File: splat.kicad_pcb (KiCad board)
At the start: 2 copper layers, 40 x 70 mm, 47 parts, among them J1 BATT, J2 EXT_SW, J3 Micro_SD_Card, J4 PYRO1, J5 PYRO3, J6 PYRO2, J7 PYRO3, J8 Conn_01x04, Q1 NTR4501NT1G, Q2 NTR4501NT1G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

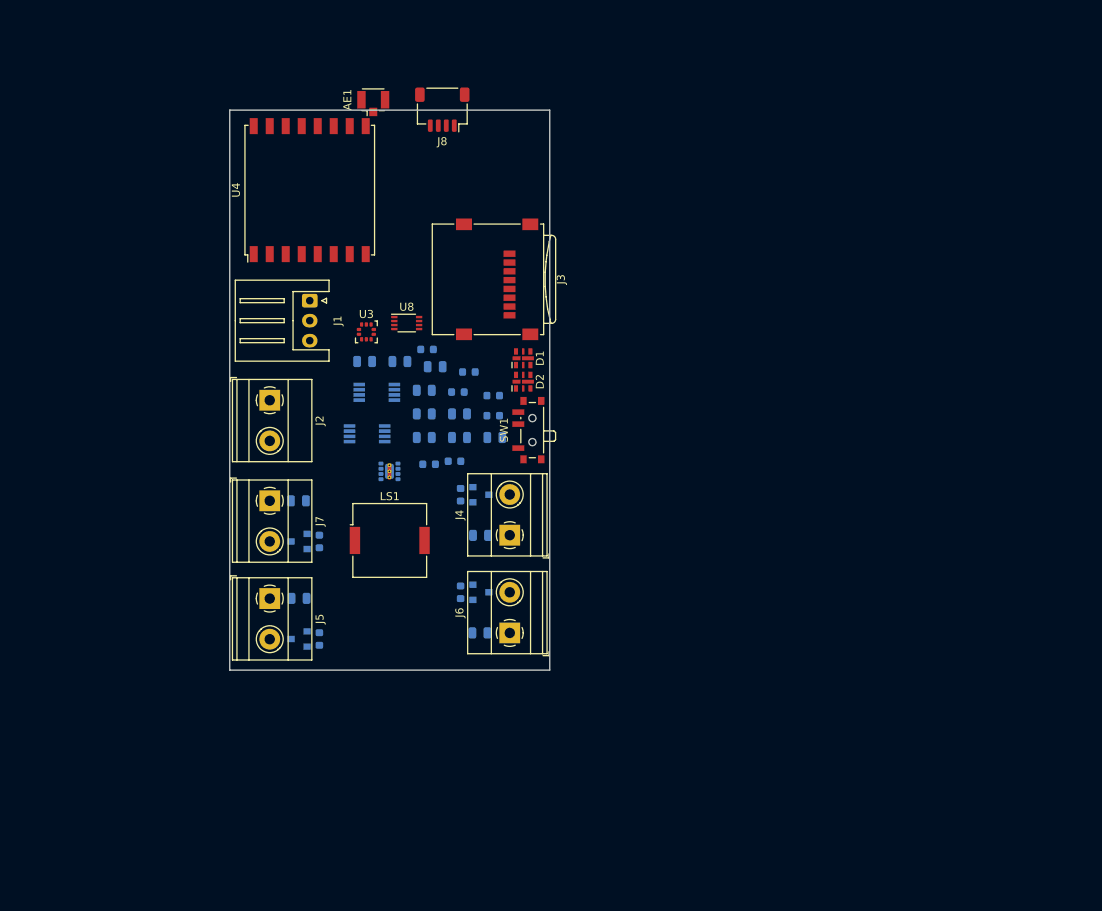
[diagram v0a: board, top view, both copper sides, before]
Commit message: Add teensy 3.6, add IMU, start connecting important nets
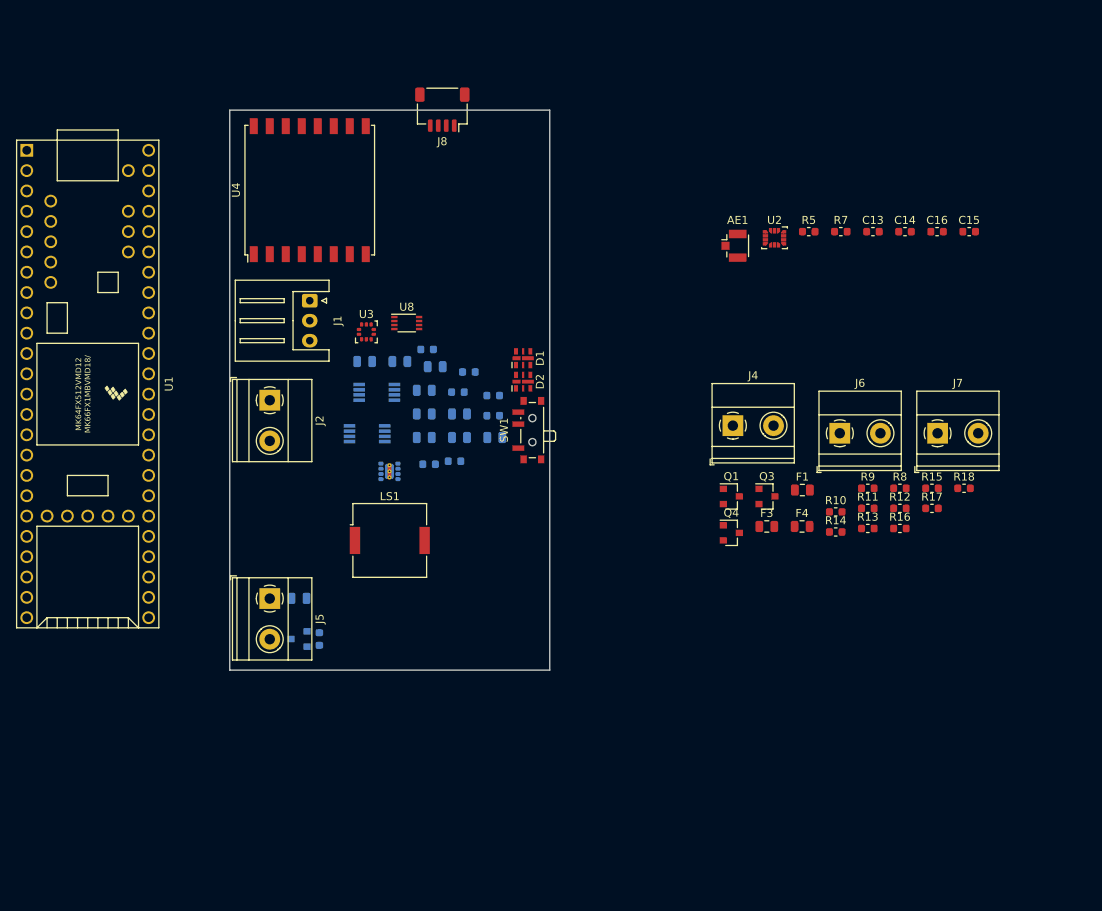
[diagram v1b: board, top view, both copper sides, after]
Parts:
- removed J3: Micro_SD_Card, Connector_Card:microSD_HC_Wuerth_693072010801
- added C13: 100nF, Capacitor_SMD:C_0603_1608Metric, F.Cu at (280.4, 75.2)
- added C14: 1uF, Capacitor_SMD:C_0603_1608Metric, F.Cu at (284.4, 75.2)
- added C15: 100nF, Capacitor_SMD:C_0603_1608Metric, F.Cu at (292.4, 75.2)
- added C16: 1uF, Capacitor_SMD:C_0603_1608Metric, F.Cu at (288.4, 75.2)
- added R10: 100K, Resistor_SMD:R_0603_1608Metric, F.Cu at (275.7, 110.2)
- added R11: 300K, Resistor_SMD:R_0603_1608Metric, F.Cu at (279.8, 109.8)
- added R12: 100K, Resistor_SMD:R_0603_1608Metric, F.Cu at (283.8, 109.8)
- added R13: 10K, Resistor_SMD:R_0603_1608Metric, F.Cu at (279.8, 112.3)
- added R14: 10K, Resistor_SMD:R_0603_1608Metric, F.Cu at (275.7, 112.7)
- added R15: 300K, Resistor_SMD:R_0603_1608Metric, F.Cu at (287.8, 107.3)
- added R16: 100K, Resistor_SMD:R_0603_1608Metric, F.Cu at (283.8, 112.3)
- added R17: 300K, Resistor_SMD:R_0603_1608Metric, F.Cu at (287.8, 109.8)
- added R18: 100K, Resistor_SMD:R_0603_1608Metric, F.Cu at (291.8, 107.3)
- added R9: 300K, Resistor_SMD:R_0603_1608Metric, F.Cu at (279.8, 107.3)
- added U1: Teensy3.6, splat:Teensy35_36, F.Cu at (182.2, 94.2)
- added U2: ISM330DLC, Package_LGA:LGA-14_3x2.5mm_P0.5mm_LayoutBorder3x4y, F.Cu at (268.1, 76.0)
- AE1: value Antenna -> Antenna_Shield
- F1, F3, F4, Q1, Q3, Q4, R7, R8: moved to F.Cu
- J7: value PYRO3 -> PYRO4
- R5: value 10K -> 1K; moved to F.Cu
- moved J7 83.9 mm to (288.5, 100.4), turned to 0 degrees
- moved R8 72.9 mm to (283.8, 107.3), turned to 0 degrees
- moved R7 65.5 mm to (276.4, 75.2), turned to 0 degrees
- moved F4 63.0 mm to (271.5, 112.0), turned to 0 degrees
- moved R5 54.5 mm to (272.4, 75.2), turned to 0 degrees
- moved Q4 54.0 mm to (262.7, 112.8), turned to 0 degrees
- moved AE1 48.5 mm to (263.0, 77.0), turned to 0 degrees
- moved J6 48.2 mm to (276.3, 100.4), turned to 0 degrees
- moved F1 40.6 mm to (271.6, 107.5)
- moved F3 38.2 mm to (267.1, 112.0)
- moved Q3 37.7 mm to (267.1, 108.3)
- moved Q1 31.3 mm to (262.7, 108.3)
- moved J4 31.1 mm to (262.9, 99.4), turned to 0 degrees
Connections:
- net /pyro/PYRO3_EN renamed /PYRO3_EN
- AE1 pad 2: (no net) -> GND
- D1 pad 1: Net-(D1-Pad1) -> /5V_SERVO
- D2 pad 1: Net-(D2-Pad1) -> /5V_SERVO
- LS1 pad 2: (no net) -> GND
- Q1 pad 1: /pyro/PYRO1_EN -> /PYRO1_EN
- Q3 pad 1: /pyro/PYRO2_EN -> /PYRO2_EN
- Q4 pad 1: /pyro/PYRO4_EN -> /PYRO4_EN
- R5 pad 1: /pyro/PYRO1_EN -> /BEEPER
- R7 pad 1: /pyro/PYRO2_EN -> /3V3_AUX
- R7 pad 2: GND -> /BMP_INT
- R8 pad 1: /pyro/PYRO4_EN -> /PYRO1_EN
- U3 pad 3: (no net) -> GND
- U3 pad 8: (no net) -> GND
- U3 pad 9: (no net) -> GND
- U8 pad 1: (no net) -> +3V3
- U8 pad 8: (no net) -> /5V_SERVO

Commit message: Start layout, add 3d files
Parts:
- C1, C10, C11, C12, C2, C3, C4, C5, C6, C7, C8, C9, F2, Q2, R1, R2, R3, R4, R6, U5, U6, U7: moved to F.Cu
- J2, J4, J5, J6, J7: footprint TerminalBlock_Phoenix:TerminalBlock_Phoenix_MKDS-1,5-2-5.08_1x02_P5.08mm_Horizontal -> TerminalBlock_Phoenix:TerminalBlock_Phoenix_PT-1,5-2-3.5-H_1x02_P3.50mm_Horizontal
- LS1: moved to B.Cu
- U1: value Teensy3.6 -> TEENSY3.6; footprint splat:Teensy35_36 -> footprints:Teensy35_36
- moved U2 66.1 mm to (202.1, 79.1)
- moved C6 64.4 mm to (226.7, 154.3)
- moved R7 55.7 mm to (232.5, 109.6), turned to 180 degrees
- moved R2 53.2 mm to (224.2, 157.5)
- moved J7 45.7 mm to (242.8, 101.4), turned to 270 degrees
- moved J1 41.9 mm to (208.3, 125.7)
- moved F3 41.3 mm to (236.0, 85.0)
- moved LS1 40.2 mm to (260.2, 114.8), turned to 270 degrees
- moved J5 39.5 mm to (242.8, 109.5)
- moved C10 39.0 mm to (221.7, 130.4), turned to 270 degrees
- moved F1 38.4 mm to (236.0, 93.2)
- moved AE1 38.0 mm to (229.0, 60.1), turned to 90 degrees
- moved SW1 37.6 mm to (201.0, 109.3), turned to 270 degrees
- moved F4 37.1 mm to (236.0, 101.3)
- moved Q3 36.9 mm to (236.0, 88.6)
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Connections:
- J1 pad 1: GND -> Net-(J1-Pad1)
- J1 pad 3: Net-(J1-Pad3) -> GND
- J2 pad 1: Net-(J1-Pad3) -> Net-(J1-Pad1)
- J8 pad 1: (no net) -> +3V3
- J8 pad 2: (no net) -> /TXD_GPS
- J8 pad 3: (no net) -> /RXD_GPS
- J8 pad 4: (no net) -> GND
- LS1 pad 1: (no net) -> /BEEPER
- U1 pad 1: Net-(U1-Pad1) -> (no net)
- U1 pad 10: Net-(U1-Pad10) -> (no net)
- U1 pad 11: Net-(U1-Pad11) -> (no net)
- U1 pad 12: Net-(U1-Pad12) -> /CS_RF
- U1 pad 13: Net-(U1-Pad13) -> /MOSI_0
- U1 pad 14: Net-(U1-Pad14) -> /MISO_0
- U1 pad 15: Net-(U1-Pad15) -> (no net)
- U1 pad 16: Net-(U1-Pad16) -> /RF_DIO0
- U1 pad 17: Net-(U1-Pad17) -> /RF_DIO1
- U1 pad 18: Net-(U1-Pad18) -> /TXD_GPS
- U1 pad 19: Net-(U1-Pad19) -> /RXD_GPS
- U1 pad 2: Net-(U1-Pad2) -> /PYRO1_EN
- U1 pad 20: Net-(U1-Pad20) -> /RF_DIO2
- U1 pad 21: Net-(U1-Pad21) -> /RF_DIO3
- U1 pad 22: Net-(U1-Pad22) -> /RF_DIO4
- U1 pad 23: Net-(U1-Pad23) -> /RF_DIO5
- U1 pad 24: Net-(U1-Pad24) -> (no net)
- U1 pad 25: Net-(U1-Pad25) -> (no net)
- U1 pad 26: Net-(U1-Pad26) -> (no net)
- U1 pad 27: Net-(U1-Pad27) -> (no net)
- U1 pad 28: Net-(U1-Pad28) -> (no net)
- U1 pad 29: Net-(U1-Pad29) -> (no net)
- U1 pad 3: Net-(U1-Pad3) -> /PYRO2_EN
- U1 pad 30: Net-(U1-Pad30) -> (no net)
- U1 pad 31: Net-(U1-Pad31) -> (no net)
- U1 pad 32: Net-(U1-Pad32) -> (no net)
- U1 pad 33: Net-(U1-Pad33) -> (no net)
- U1 pad 34: Net-(U1-Pad34) -> (no net)
- U1 pad 35: Net-(U1-Pad35) -> (no net)
- U1 pad 36: Net-(U1-Pad36) -> /BMP_INT
- U1 pad 37: Net-(U1-Pad37) -> (no net)
- U1 pad 38: Net-(U1-Pad38) -> (no net)
- U1 pad 39: Net-(U1-Pad39) -> (no net)
- U1 pad 4: Net-(U1-Pad4) -> /PYRO3_EN
- U1 pad 40: Net-(U1-Pad40) -> (no net)
- U1 pad 41: Net-(U1-Pad41) -> /PYRO4_SENSE
- U1 pad 42: Net-(U1-Pad42) -> /PYRO3_SENSE
- U1 pad 43: Net-(U1-Pad43) -> /PYRO2_SENSE
- U1 pad 44: Net-(U1-Pad44) -> /PYRO1_SENSE
- U1 pad 45: Net-(U1-Pad45) -> (no net)
- U1 pad 46: Net-(U1-Pad46) -> (no net)
- U1 pad 47: Net-(U1-Pad47) -> /IMU_INT2
- U1 pad 48: Net-(U1-Pad48) -> /IMU_INT1
- U1 pad 49: Net-(U1-Pad49) -> (no net)
- U1 pad 5: Net-(U1-Pad5) -> /PYRO4_EN
- U1 pad 50: Net-(U1-Pad50) -> (no net)
- U1 pad 51: Net-(U1-Pad51) -> (no net)
- U1 pad 52: Net-(U1-Pad52) -> (no net)
- U1 pad 53: Net-(U1-Pad53) -> (no net)
- U1 pad 54: Net-(U1-Pad54) -> (no net)
- U1 pad 55: Net-(U1-Pad55) -> (no net)
- U1 pad 56: Net-(U1-Pad56) -> (no net)
- U1 pad 57: Net-(U1-Pad57) -> (no net)
- U1 pad 6: Net-(U1-Pad6) -> (no net)
- U1 pad 7: Net-(U1-Pad7) -> (no net)
- U1 pad 8: Net-(U1-Pad8) -> (no net)
- U1 pad 9: Net-(U1-Pad9) -> (no net)
- U2 pad 1: Net-(U2-Pad1) -> (no net)
- U2 pad 10: Net-(U2-Pad10) -> (no net)
- U2 pad 11: Net-(U2-Pad11) -> (no net)
- U2 pad 12: Net-(U2-Pad12) -> (no net)
- U2 pad 13: /I2C1_SCL -> (no net)
- U2 pad 14: /I2C1_SDA -> (no net)
- U2 pad 2: Net-(U2-Pad2) -> (no net)
- U2 pad 3: Net-(U2-Pad3) -> (no net)
- U3 pad 7: (no net) -> /BMP_INT
- U4 pad 11: (no net) -> /RF_DIO3
- U4 pad 12: (no net) -> /RF_DIO4
- U4 pad 14: (no net) -> /RF_DIO0
- U4 pad 15: (no net) -> /RF_DIO1
- U4 pad 16: (no net) -> /RF_DIO2
- U4 pad 2: (no net) -> /MISO_0
- U4 pad 3: (no net) -> /MOSI_0
- U4 pad 5: (no net) -> /CS_RF
- U4 pad 7: (no net) -> /RF_DIO5
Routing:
- net Net-(R3-Pad2): track 0.00 -> 5.37 mm
- net GND: track 0.00 -> 3.77 mm
- net Net-(C4-Pad1): track 0.00 -> 1.78 mm
- added copper zone on F.Cu, net +BATT
- added copper zone on F.Cu, net /5V_SERVO
- added copper zone on F.Cu, net GND
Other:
- board size 40 x 70 mm -> 49.5 x 76.8 mm
- net class Default: clearance 0.2 -> 0.1524; trace_width 0.25 -> 0.1524; via_dia 0.8 -> 0.762; via_drill 0.4 -> 0.381
- rule trace_clearance: 0.2 -> 0.1524
- rule trace_min: 0.2 -> 0.1524
- rule via_min_drill: 0.3 -> 0.3302
- rule via_min_size: 0.4 -> 0.381

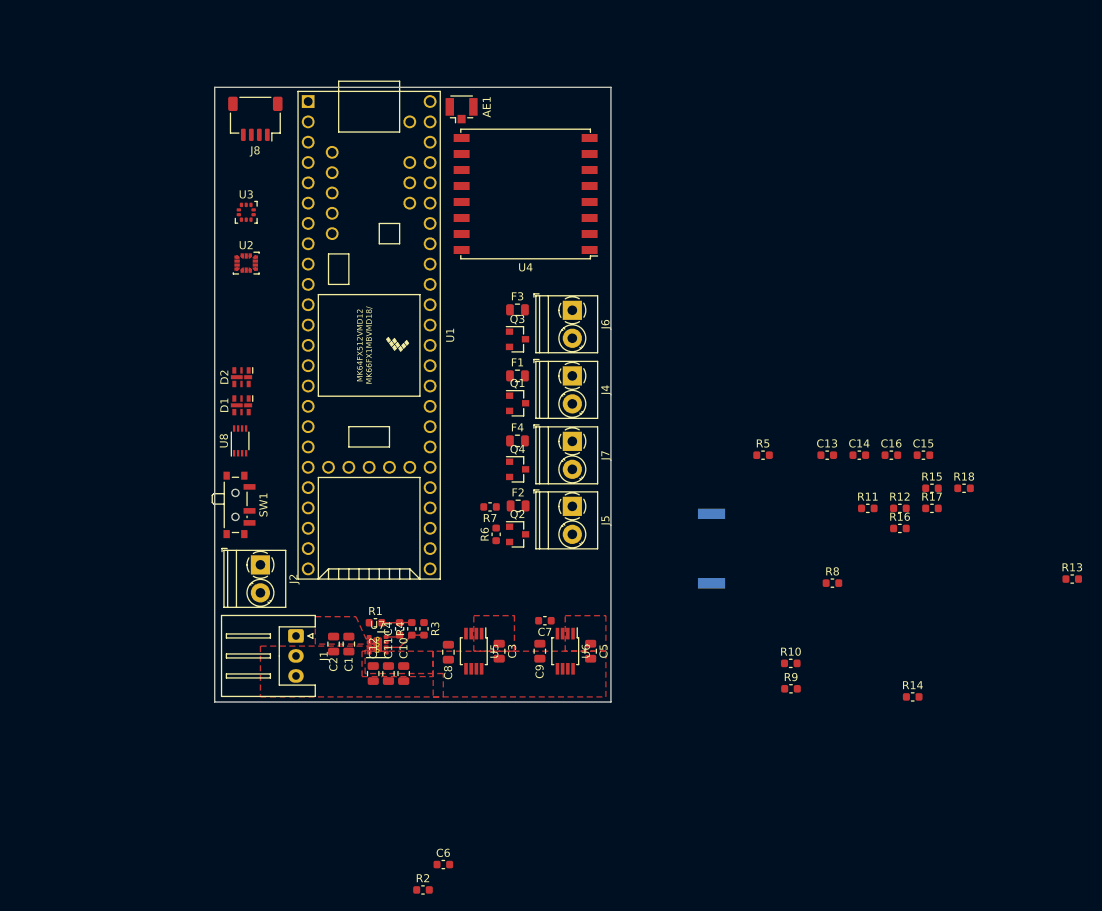
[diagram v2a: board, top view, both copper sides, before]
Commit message: Layout and servo connectors
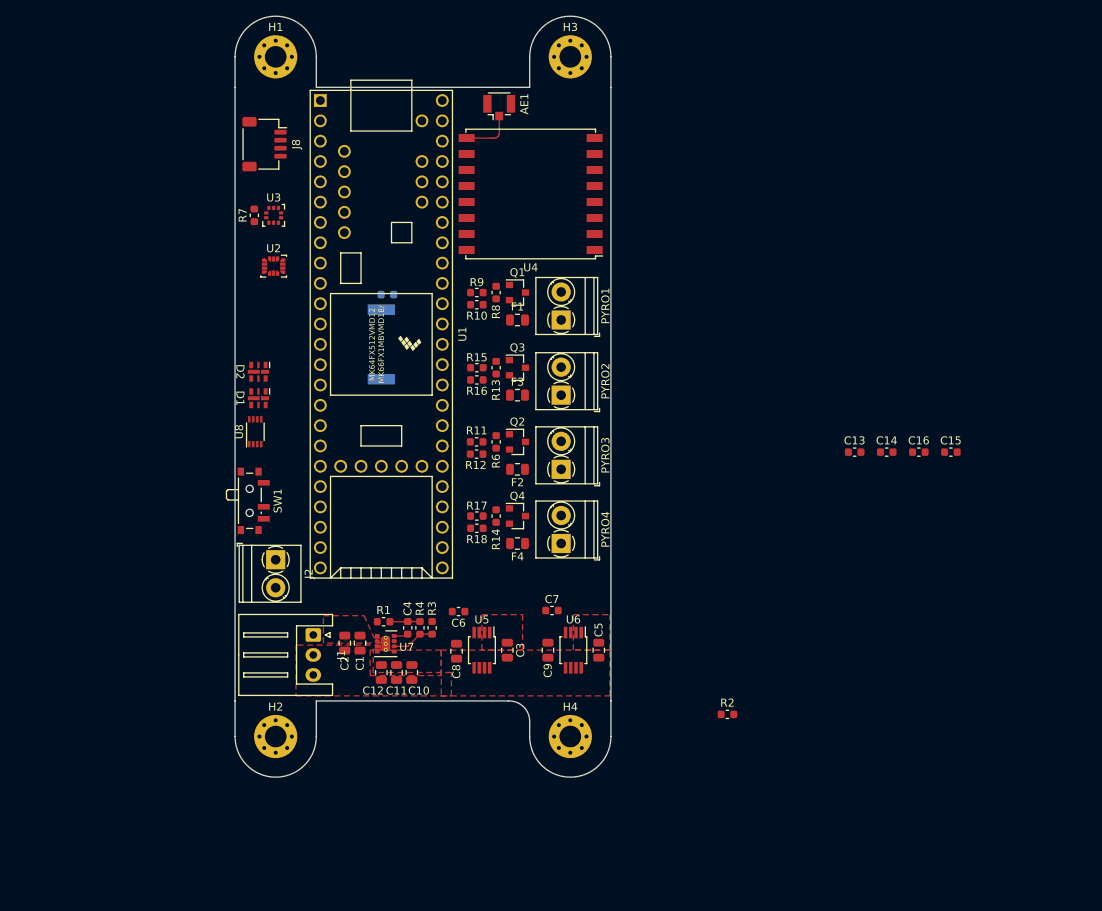
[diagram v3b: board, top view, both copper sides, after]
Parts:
- added H1: MountingHole_Pad, MountingHole:MountingHole_2.7mm_Pad_Via, F.Cu at (205.7, 53.3)
- added H2: MountingHole_Pad, MountingHole:MountingHole_2.7mm_Pad_Via, F.Cu at (205.7, 138.3)
- added H3: MountingHole_Pad, MountingHole:MountingHole_2.7mm_Pad_Via, F.Cu at (242.6, 53.3)
- added H4: MountingHole_Pad, MountingHole:MountingHole_2.7mm_Pad_Via, F.Cu at (242.6, 138.3)
- R5: moved to B.Cu
- moved R13 76.7 mm to (233.3, 92.2), turned to 270 degrees
- moved R9 63.2 mm to (230.9, 82.8), turned to 180 degrees
- moved R18 61.1 mm to (230.9, 112.3)
- moved R10 59.6 mm to (230.9, 84.3)
- moved R15 58.9 mm to (230.9, 92.2), turned to 180 degrees
- moved R17 56.9 mm to (230.9, 110.7), turned to 180 degrees
- moved R14 56.8 mm to (233.3, 110.7), turned to 270 degrees
- moved R16 56.0 mm to (230.9, 93.7)
- moved R8 55.6 mm to (233.3, 82.8), turned to 270 degrees
- moved R12 53.3 mm to (230.9, 103.0)
- moved R5 51.1 mm to (219.7, 83.1)
- moved R11 49.6 mm to (230.9, 101.5), turned to 180 degrees
- moved LS1 48.5 mm to (218.9, 89.3)
- moved R7 46.9 mm to (203.1, 73.2), turned to 90 degrees
- moved R2 43.9 mm to (262.2, 135.5)
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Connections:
- U1 pad 1: (no net) -> GND
- U1 pad 16: /RF_DIO0 -> (no net)
- U1 pad 17: /RF_DIO1 -> (no net)
- U1 pad 20: /RF_DIO2 -> (no net)
- U1 pad 21: /RF_DIO3 -> (no net)
- U1 pad 22: /RF_DIO4 -> (no net)
- U1 pad 23: /RF_DIO5 -> (no net)
- U1 pad 27: (no net) -> GND
- U1 pad 37: (no net) -> /PYRO4_SENSE
- U1 pad 38: (no net) -> /PYRO3_SENSE
- U1 pad 39: (no net) -> GND
- U1 pad 41: /PYRO4_SENSE -> /PYRO2_SENSE
- U1 pad 42: /PYRO3_SENSE -> /PYRO1_SENSE
- U1 pad 43: /PYRO2_SENSE -> /IMU_INT2
- U1 pad 44: /PYRO1_SENSE -> /IMU_INT1
- U1 pad 47: /IMU_INT2 -> /RF_DIO5
- U1 pad 48: /IMU_INT1 -> /RF_DIO4
- U1 pad 49: (no net) -> /RF_DIO3
- U1 pad 50: (no net) -> /RF_DIO2
- U1 pad 52: (no net) -> GND
- U1 pad 56: (no net) -> /RF_DIO1
- U1 pad 57: (no net) -> /RF_DIO0
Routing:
- net Net-(AE1-Pad1): track 0.00 -> 6.76 mm
- added copper zone on In1.Cu, net GND
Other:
- board size 49.5 x 76.8 mm -> 47 x 95.1 mm
- copper layers 2 -> 4
